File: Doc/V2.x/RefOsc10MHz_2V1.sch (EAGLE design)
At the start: 77 parts, among them CON1 TYCO-AMP_USBUSB-B_SMT, CON11 MCX-J-P-X-RA-SM1, CON2 HEADER-2X5SMD, CON3 SD-73100-0105, CON4 AVR-ISP-6SMD, CON5 AVR-JTAG-10SMD, CON6 HEADER-2X3SMD, IC1 ATmega328-P, IC11 712-RXM-GNSS-TM-B, IC2 LC4032V_XXT44, IC3 74HCT221D, IC4 CFPT-141, IC5 LMH6645MF, IC6 LM2831YMF

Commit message: avr_DF4IAH_Bootloader - Doc - Eagle: V2.1 - OP-Amps U4 and U5 added/changed
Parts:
- removed IC5: LMH6645MF, df4iah:LMH6645MF
- added C941: 100n, rcl:C-EUC0805
- added R941: 10k, rcl:R-EU_R0805
- added R942: 22k, rcl:R-EU_R0805
- added TP235: TPTP15R, testpad:TPTP15R
- added U4: OPA357, df4iah_opamp:OPA357
- added U5: OPA354, df4iah_opamp:OPA354
- C71: value 10p -> 0p
- C911, C921, C922, C931, C951: value 10n -> 100n
- R221: value 56 -> 68
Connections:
- net GATE renamed GATE_IN
- net GATE_TRIG renamed GATE_TRIG_OUT
- net SYNC renamed SYNC_IN
- new net N$6: R941.2, R942.1, U4.-IN
- new net OP_ENA: IC2.IOB8, U4.ENABLE
- new net OP_IN: IC2.IOB9, U4.+IN
- new net PHASE_OUT: IC2.IOB12, TP235.TP
- net ADC_PHASE: now also U5.-IN, U5.OUT; no longer IC5.VIN-, IC5.VOUT
- net ADC_PHASE_PULLHOLD: now also U5.+IN; no longer IC5.VIN+
- net GND: now also C941.2, R941.1, U4.V-, U5.V-; no longer IC5.-VS
- net PHASE_ERROR: now also U4.OUT; no longer IC2.IOB12
- net VCC: now also C941.1, R942.2, U4.V+, U5.V+; no longer IC5.VS+
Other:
- note added: "S & H"
- note removed: "Gate Trig out"
- note removed: "Gate in"
- note removed: "Phase out"
- note removed: "Phase-Error"
- note removed: "Pull & Hold"
- note removed: "Sync in"

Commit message: avr_DF4IAH_Bootloader - Doc - Eagle: V2.1 - Sample&Hold - reduce from 10nF to 100pF, components are renamed
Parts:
- removed C1: 47uF, rcl:CPOL-EUC
- removed C81: 0.22F, rcl:CPOL-EU140CLH-1010
- added C191, C291: 100n, rcl:C-EUC0805
- added R421, R501: 27, rcl:R-EU_R0805
- C591: value 100n -> 10n
- C911: value 100n -> 47uF; device rcl:C-EUC0805 -> rcl:CPOL-EUC
- C921: value 100n -> 0.22F; device rcl:C-EUC0805 -> rcl:CPOL-EU140CLH-1010
- renumbered C111 to C891, C2 to C912, C203 to C611, C21 to C152, C212 to C613, C213 to C612, C22 to C151, C221 to C791, C31 to C101, C32 to C102, C51 to C411, C71 to C301, C72 to C311, C922 to C292, C931 to C391, C941 to C491, C951 to C591, CON11 to CON7, D1 to D911, D2 to D912, D201 to D151, D202 to D152, D211 to D611, D221 to D701, D82 to D921, H1 to H904, H2 to H901, H3 to H902, H4 to H903, IC11 to IC8, IC4 to IC7, JP1 to JP111, JP2 to JP941, JP3 to JP121, L211 to L611, L31 to L101, LFP111 to LFP811, R1 to R916, R13 to R151, R2 to R915, R21 to R121, R211 to R612, R212 to R611, R213 to R601, R22 to R122, R221 to R701, R23 to R123, R25 to R201, R3 to R914, R31 to R131, R4 to R913, R41 to R111, R51 to R411, R52 to R141, R61 to R931, R71 to R301, R72 to R311, R81 to R951, R941 to R401, R942 to R402, SJ21 to SJ201, SJ22 to SJ202
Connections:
- net ADC_PHASE_PULLHOLD renamed ADC_PHASE_SAMPLEHOLD
- new net OP_IN_R: R421.2, U4.+IN
- new net U5_FB: R501.2, U5.-IN
- net +3V3: now also C291.1; no longer C921.1
- net ADC_PHASE: now also R501.1; no longer U5.-IN
- net GND: now also C191.2, C291.2, C911.-, C921.-; no longer C1.-, C81.-, C911.2, C921.2
- net GPS_VBACKUP: now also C921.+; no longer C81.+
- net OP_IN: now also R421.1; no longer U4.+IN
- net VCC: now also C191.1, C911.+; no longer C1.+, C911.1

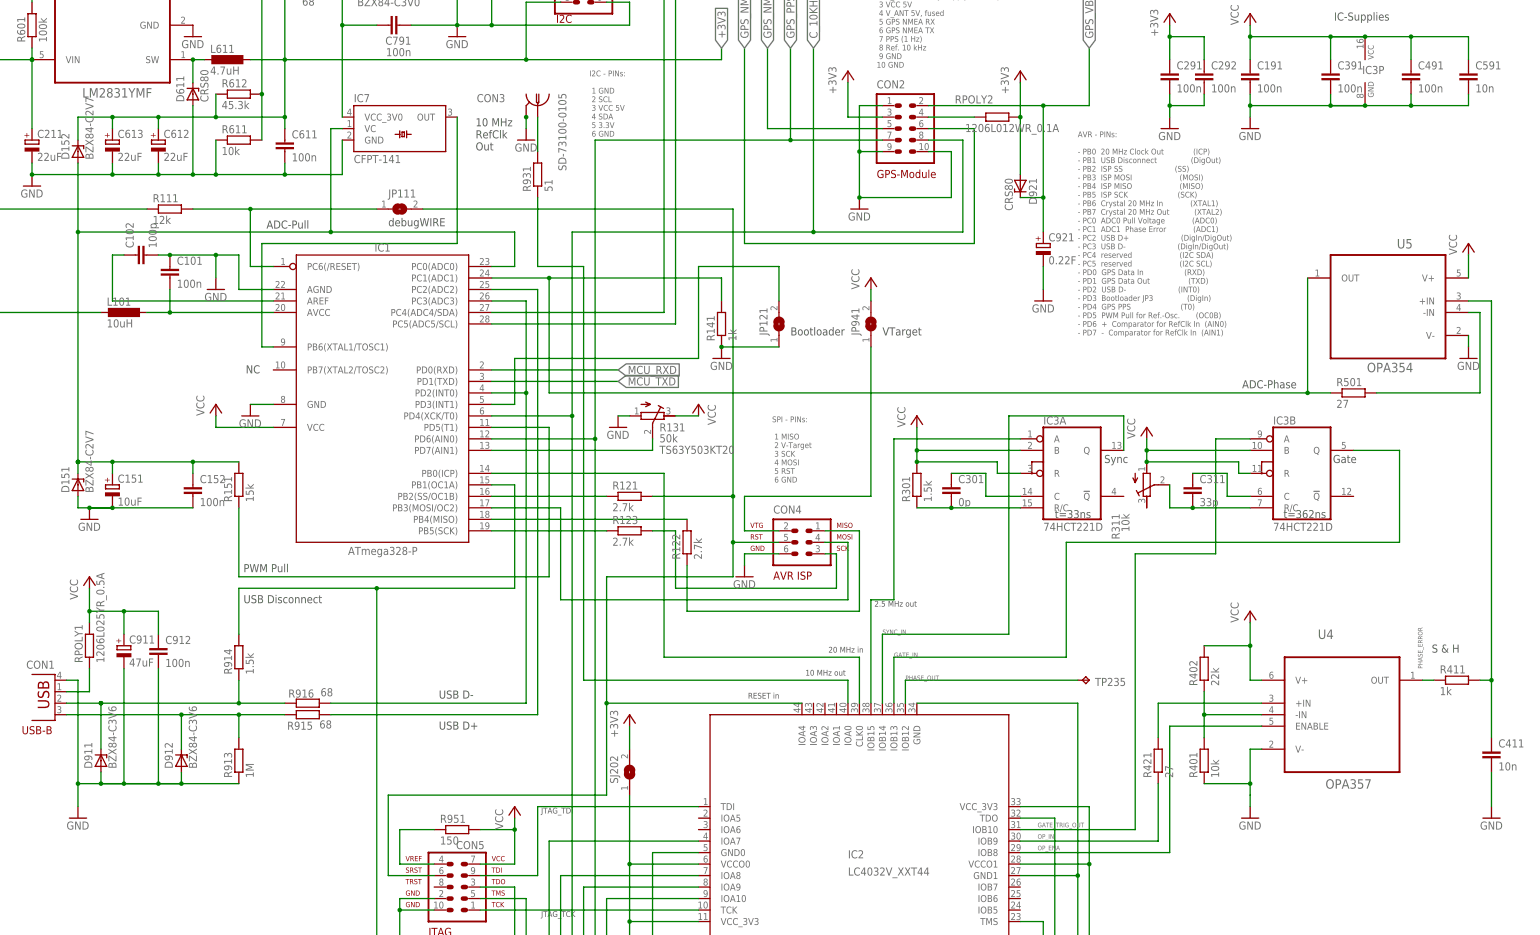
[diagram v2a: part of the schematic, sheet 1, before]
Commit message: avr_DF4IAH_Bootloader - Doc - Eagle: V2.1 - Sample&Hold - reduce from 10nF to 100pF, components are renamed (2)
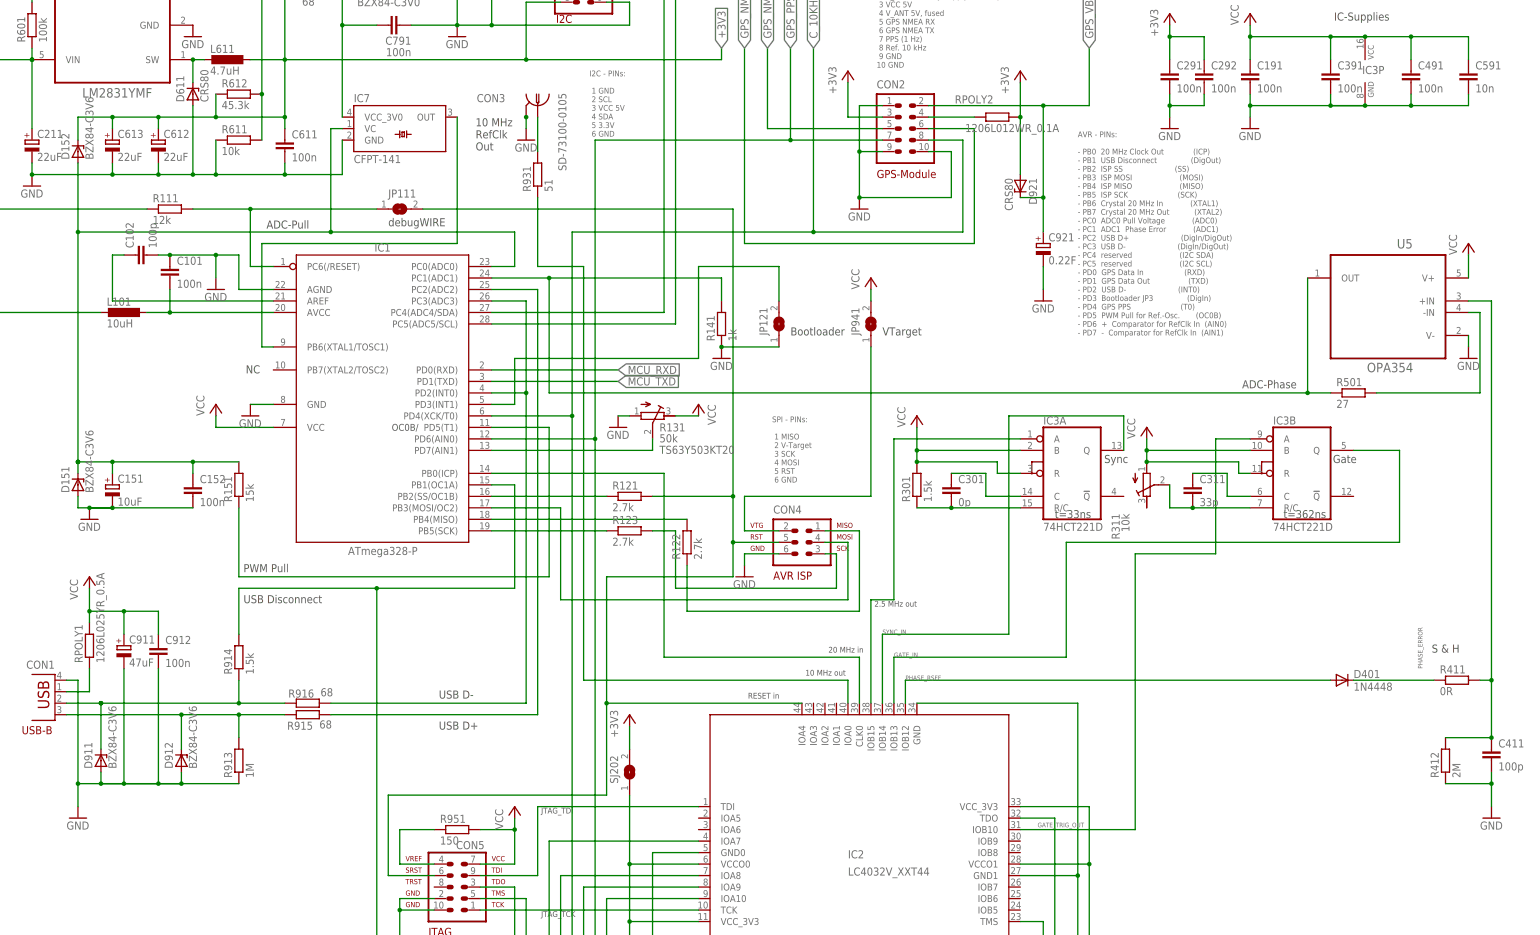
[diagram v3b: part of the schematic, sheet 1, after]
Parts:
- removed R401: 10k, rcl:R-EU_R0805
- removed R402: 22k, rcl:R-EU_R0805
- removed R421: 27, rcl:R-EU_R0805
- removed TP235: TPTP15R, testpad:TPTP15R
- removed U4: OPA357, df4iah_opamp:OPA357
- added D401: 1N4448, diode:DIODE-SOD123
- added R412: 2M, rcl:R-EU_R0805
- C411: value 10n -> 100p
- D151, D152: value BZX84-C2V7 -> BZX84-C3V6
- R411: value 1k -> 0R
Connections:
- removed net N$6: R401.2, R402.1, U4.-IN
- removed net OP_ENA: IC2.IOB8, U4.ENABLE
- removed net OP_IN: IC2.IOB9, R421.1
- removed net OP_IN_R: R421.2, U4.+IN
- removed net PHASE_OUT: IC2.IOB12, TP235.TP
- new net PHASE_RSFF: D401.A, IC2.IOB12
- net ADC_PHASE_SAMPLEHOLD: now also R412.2
- net GND: now also R412.1; no longer R401.1, U4.V-
- net PHASE_ERROR: now also D401.C; no longer U4.OUT
- net VCC: no longer R402.2, U4.V+
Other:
- note added: "OC0B/"
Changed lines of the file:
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@@
 <part name="D911" library="diode" deviceset="BZX84CSMD" device="" value="BZX84-C3V6"/>
 <part name="D912" library="diode" deviceset="BZX84CSMD" device="" value="BZX84-C3V6"/>
-<part name="D151" library="diode" deviceset="BZX84CSMD" device="" value="BZX84-C2V7"/>
-<part name="D152" library="diode" deviceset="BZX84CSMD" device="" value="BZX84-C2V7"/>
+<part name="D151" library="diode" deviceset="BZX84CSMD" device="" value="BZX84-C3V6"/>
+<part name="D152" library="diode" deviceset="BZX84CSMD" device="" value="BZX84-C3V6"/>
 <part name="RPOLY1" library="rcl" deviceset="R-EU_" device="M1206" value="1206L025YR_0.5A"/>
 <part name="RPOLY2" library="rcl" deviceset="R-EU_" device="M1206" value="1206L012WR_0.1A"/>
@@
 <part name="R111" library="rcl" deviceset="R-EU_" device="R0805" value="12k"/>
 <part name="R931" library="rcl" deviceset="R-EU_" device="R0805" value="51"/>
-<part name="R411" library="rcl" deviceset="R-EU_" device="R0805" value="1k"/>
+<part name="R411" library="rcl" deviceset="R-EU_" device="R0805" value="0R"/>
 <part name="R141" library="rcl" deviceset="R-EU_" device="R0805" value="1k"/>
 <part name="R301" library="rcl" deviceset="R-EU_" device="R0805" value="1.5k"/>
@@
 <part name="C611" library="rcl" deviceset="C-EU" device="C0805" value="100n"/>
 <part name="C102" library="rcl" deviceset="C-EU" device="C0805" value="100p"/>
-<part name="C411" library="rcl" deviceset="C-EU" device="C0805" value="10n"/>
+<part name="C411" library="rcl" deviceset="C-EU" device="C0805" value="100p"/>
 <part name="C301" library="rcl" deviceset="C-EU" device="C0805" value="0p"/>
 <part name="C311" library="rcl" deviceset="C-EU" device="C0805" value="33p"/>
@@
 <part name="D701" library="diode" deviceset="BZX84CSMD" device="" value="BZX84-C3V0"/>
 <part name="R701" library="rcl" deviceset="R-EU_" device="R0805" value="68"/>
-<part name="TP235" library="testpad" deviceset="TP" device="TP15R"/>
-<part name="U4" library="df4iah_opamp" deviceset="OPA357" device=""/>
-<part name="GND25" library="supply1" deviceset="GND" device=""/>
-<part name="P+10" library="supply1" deviceset="VCC" device=""/>
 <part name="C491" library="rcl" deviceset="C-EU" device="C0805" value="100n"/>
-<part name="R401" library="rcl" deviceset="R-EU_" device="R0805" value="10k"/>
-<part name="R402" library="rcl" deviceset="R-EU_" device="R0805" value="22k"/>
 <part name="U5" library="df4iah_opamp" deviceset="OPA354" device=""/>
 <part name="R501" library="rcl" deviceset="R-EU_" device="R0805" value="27"/>
-<part name="R421" library="rcl" deviceset="R-EU_" device="R0805" value="27"/>
+<part name="R412" library="rcl" deviceset="R-EU_" device="R0805" value="2M"/>
+<part name="D401" library="diode" deviceset="DIODE-" device="SOD123" value="1N4448"/>
 </parts>
 <sheets>
@@
  6 GND</text>
 <text x="133.604" y="239.268" size="1.778" layer="94">I2C</text>
+<text x="97.282" y="149.098" size="1.524" layer="97">OC0B/</text>
 </plain>
 <instances>
@@
 </instance>
 <instance part="R701" gate="G$1" x="81.28" y="246.38"/>
-<instance part="TP235" gate="G$1" x="251.46" y="93.98" smashed="yes" rot="R270">
-<attribute name="NAME" x="252.73" y="92.71" size="1.778" layer="95"/>
-<attribute name="TP_SIGNAL_NAME" x="250.19" y="92.71" size="1.778" layer="97" rot="R270"/>
-</instance>
-<instance part="U4" gate="A" x="307.34" y="88.9"/>
-<instance part="GND25" gate="1" x="287.02" y="63.5"/>
-<instance part="P+10" gate="VCC" x="287.02" y="109.22"/>
 <instance part="C491" gate="G$1" x="322.58" y="228.6"/>
-<instance part="R401" gate="G$1" x="276.86" y="76.2" rot="R90"/>
-<instance part="R402" gate="G$1" x="276.86" y="96.52" rot="R90"/>
 <instance part="U5" gate="A" x="317.5" y="180.34" rot="MR0"/>
 <instance part="R501" gate="G$1" x="309.88" y="157.48"/>
-<instance part="R421" gate="G$1" x="266.7" y="76.2" rot="R90"/>
+<instance part="R412" gate="G$1" x="330.2" y="76.2" rot="R90"/>
+<instance part="D401" gate="G$1" x="307.34" y="93.98"/>
 </instances>
 <busses>
@@
 <segment>
 <pinref part="GND14" gate="1" pin="GND"/>
-<wire x1="340.36" y1="66.04" x2="340.36" y2="73.66" width="0.1524" layer="91"/>
+<wire x1="340.36" y1="66.04" x2="340.36" y2="71.12" width="0.1524" layer="91"/>
 <pinref part="C411" gate="G$1" pin="2"/>
+<pinref part="R412" gate="G$1" pin="1"/>
+<wire x1="340.36" y1="71.12" x2="340.36" y2="73.66" width="0.1524" layer="91"/>
+<wire x1="340.36" y1="71.12" x2="330.2" y2="71.12" width="0.1524" layer="91"/>
+<junction x="340.36" y="71.12"/>
 </segment>
 <segment>
@@
 <pinref part="D701" gate="G$1" pin="A"/>
 </segment>
-<segment>
-<pinref part="GND25" gate="1" pin="GND"/>
-<pinref part="U4" gate="A" pin="V-"/>
-<wire x1="287.02" y1="66.04" x2="287.02" y2="68.58" width="0.1524" layer="91"/>
-<wire x1="287.02" y1="71.12" x2="287.02" y2="78.74" width="0.1524" layer="91"/>
-<wire x1="287.02" y1="78.74" x2="289.56" y2="78.74" width="0.1524" layer="91"/>
-<pinref part="R401" gate="G$1" pin="1"/>
-<wire x1="287.02" y1="68.58" x2="287.02" y2="71.12" width="0.1524" layer="91"/>
-<wire x1="287.02" y1="71.12" x2="276.86" y2="71.12" width="0.1524" layer="91"/>
-<junction x="287.02" y="71.12"/>
-</segment>
 </net>
 <net name="VCC" class="2">
@@
 <wire x1="127" y1="246.38" x2="127" y2="251.46" width="0.1524" layer="91"/>
 <pinref part="P+8" gate="VCC" pin="VCC"/>
-</segment>
-<segment>
-<pinref part="P+10" gate="VCC" pin="VCC"/>
-<pinref part="U4" gate="A" pin="V+"/>
-<wire x1="287.02" y1="106.68" x2="287.02" y2="101.6" width="0.1524" layer="91"/>
-<wire x1="287.02" y1="101.6" x2="287.02" y2="93.98" width="0.1524" layer="91"/>
-<wire x1="287.02" y1="93.98" x2="289.56" y2="93.98" width="0.1524" layer="91"/>
-<pinref part="R402" gate="G$1" pin="2"/>
-<wire x1="287.02" y1="101.6" x2="276.86" y2="101.6" width="0.1524" layer="91"/>
-<junction x="287.02" y="101.6"/>
 </segment>
 </net>
@@
 <pinref part="C411" gate="G$1" pin="1"/>
 <pinref part="U5" gate="A" pin="+IN"/>
+<pinref part="R412" gate="G$1" pin="2"/>
+<wire x1="340.36" y1="81.28" x2="330.2" y2="81.28" width="0.1524" layer="91"/>
+<junction x="340.36" y="81.28"/>
 </segment>
 </net>
@@
 <segment>
 <pinref part="R411" gate="G$1" pin="1"/>
-<pinref part="U4" gate="A" pin="OUT"/>
-<wire x1="327.66" y1="93.98" x2="325.12" y2="93.98" width="0.1524" layer="91"/>
+<wire x1="327.66" y1="93.98" x2="309.88" y2="93.98" width="0.1524" layer="91"/>
 <label x="325.12" y="96.52" size="1.016" layer="95" rot="R90"/>
+<pinref part="D401" gate="G$1" pin="C"/>
 </segment>
 </net>
@@
 </segment>
 </net>
-<net name="OP_IN" class="0">
-<segment>
-<pinref part="IC2" gate="G$1" pin="IOB9"/>
-<wire x1="236.22" y1="58.42" x2="266.7" y2="58.42" width="0.1524" layer="91"/>
-<label x="240.03" y="58.928" size="1.016" layer="95"/>
-<pinref part="R421" gate="G$1" pin="1"/>
-<wire x1="266.7" y1="58.42" x2="266.7" y2="71.12" width="0.1524" layer="91"/>
-</segment>
-</net>
-<net name="OP_ENA" class="0">
-<segment>
-<pinref part="IC2" gate="G$1" pin="IOB8"/>
-<wire x1="236.22" y1="55.88" x2="269.24" y2="55.88" width="0.1524" layer="91"/>
-<wire x1="269.24" y1="55.88" x2="269.24" y2="83.82" width="0.1524" layer="91"/>
-<pinref part="U4" gate="A" pin="ENABLE"/>
-<wire x1="269.24" y1="83.82" x2="289.56" y2="83.82" width="0.1524" layer="91"/>
-<label x="240.03" y="56.388" size="1.016" layer="95"/>
-</segment>
-</net>
-<net name="N$6" class="0">
-<segment>
-<pinref part="R401" gate="G$1" pin="2"/>
-<pinref part="R402" gate="G$1" pin="1"/>
-<wire x1="276.86" y1="81.28" x2="276.86" y2="86.36" width="0.1524" layer="91"/>
-<pinref part="U4" gate="A" pin="-IN"/>
-<wire x1="276.86" y1="86.36" x2="276.86" y2="91.44" width="0.1524" layer="91"/>
-<wire x1="276.86" y1="86.36" x2="289.56" y2="86.36" width="0.1524" layer="91"/>
-<junction x="276.86" y="86.36"/>
-</segment>
-</net>
-<net name="PHASE_OUT" class="0">
+<net name="PHASE_RSFF" class="0">
 <segment>
 <wire x1="210.82" y1="93.98" x2="210.82" y2="88.9" width="0.1524" layer="91"/>
 <pinref part="IC2" gate="G$1" pin="IOB12"/>
-<wire x1="210.82" y1="93.98" x2="248.92" y2="93.98" width="0.1524" layer="91"/>
-<pinref part="TP235" gate="G$1" pin="TP"/>
+<wire x1="210.82" y1="93.98" x2="304.8" y2="93.98" width="0.1524" layer="91"/>
 <label x="210.82" y="93.98" size="1.016" layer="95"/>
+<pinref part="D401" gate="G$1" pin="A"/>
 </segment>
 </net>
@@
 </segment>
 </net>
-<net name="OP_IN_R" class="0">
-<segment>
-<pinref part="U4" gate="A" pin="+IN"/>
-<wire x1="266.7" y1="88.9" x2="289.56" y2="88.9" width="0.1524" layer="91"/>
-<pinref part="R421" gate="G$1" pin="2"/>
-<wire x1="266.7" y1="88.9" x2="266.7" y2="81.28" width="0.1524" layer="91"/>
-</segment>
-</net>
